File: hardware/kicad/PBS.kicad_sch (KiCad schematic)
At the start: 8 parts

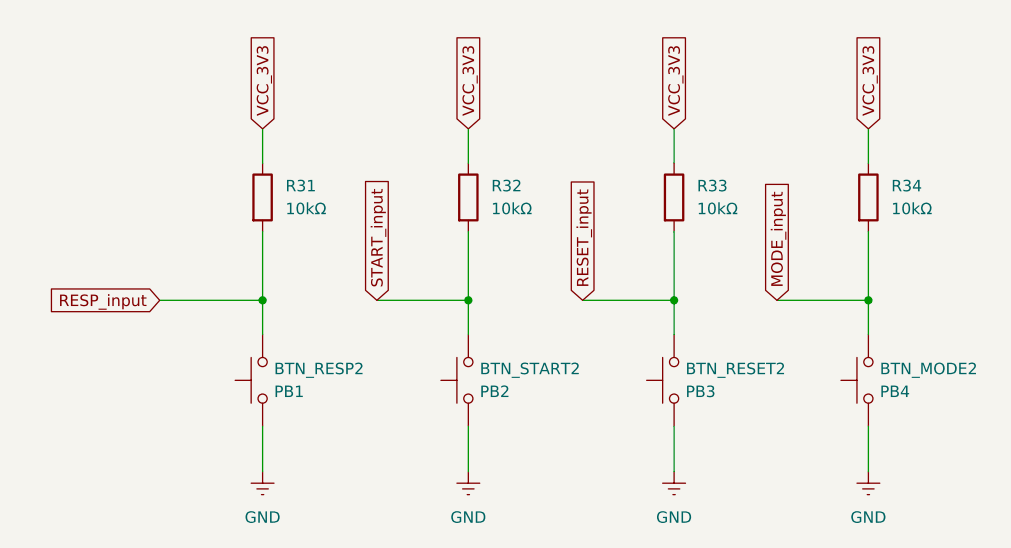
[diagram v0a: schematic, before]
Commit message: KiCad v0.2: pinout ESP32 DevKit 30 pines, botones con pull-up interna, buzzer a 5 V, resistencias SMD, logo
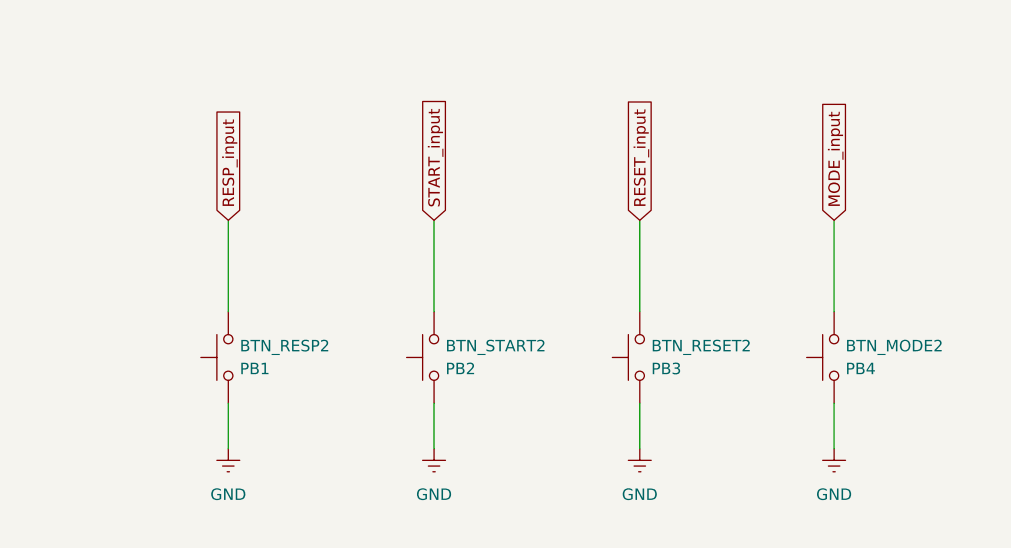
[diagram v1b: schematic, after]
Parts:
- removed R31, R32, R33, R34: 10kΩ, Resistor_THT:R_Axial_DIN0207_L6.3mm_D2.5mm_P10.16mm_Horizontal, symbol Device:R
- BTN_MODE2, BTN_RESET2, BTN_RESP2, BTN_START2: footprint Button_Switch_THT:SW_PUSH_6mm -> Connector_Molex:Molex_KK-254_AE-6410-02A_1x02_P2.54mm_Vertical
